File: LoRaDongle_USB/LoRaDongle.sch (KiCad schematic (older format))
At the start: 4 parts

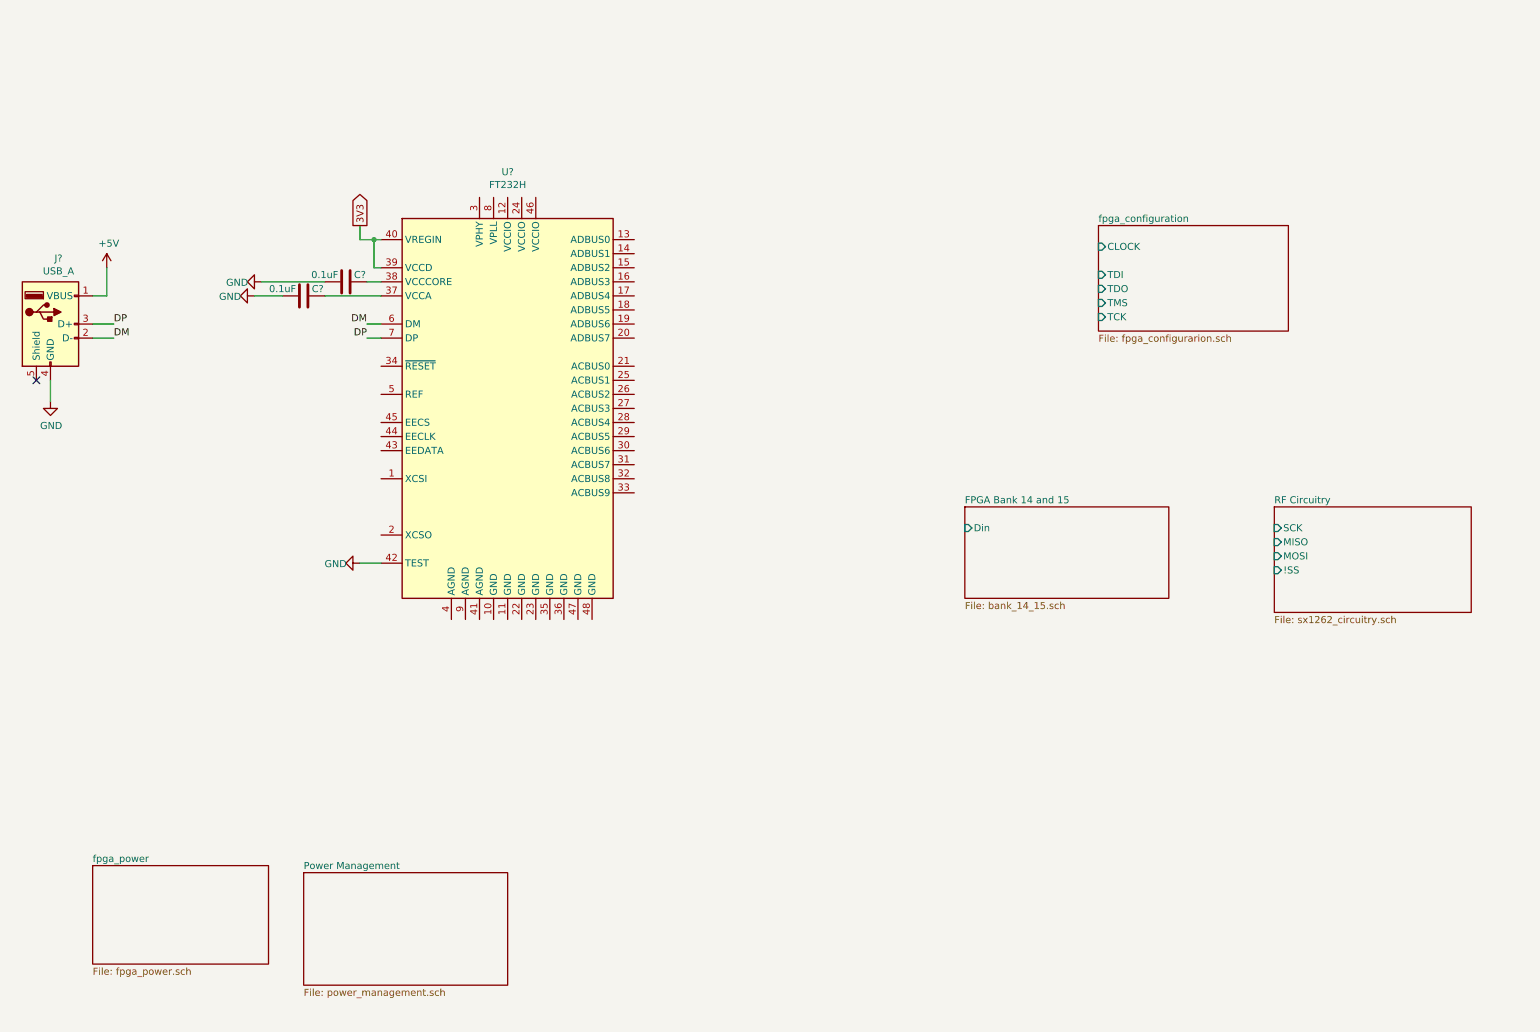
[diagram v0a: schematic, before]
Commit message: add eeprom
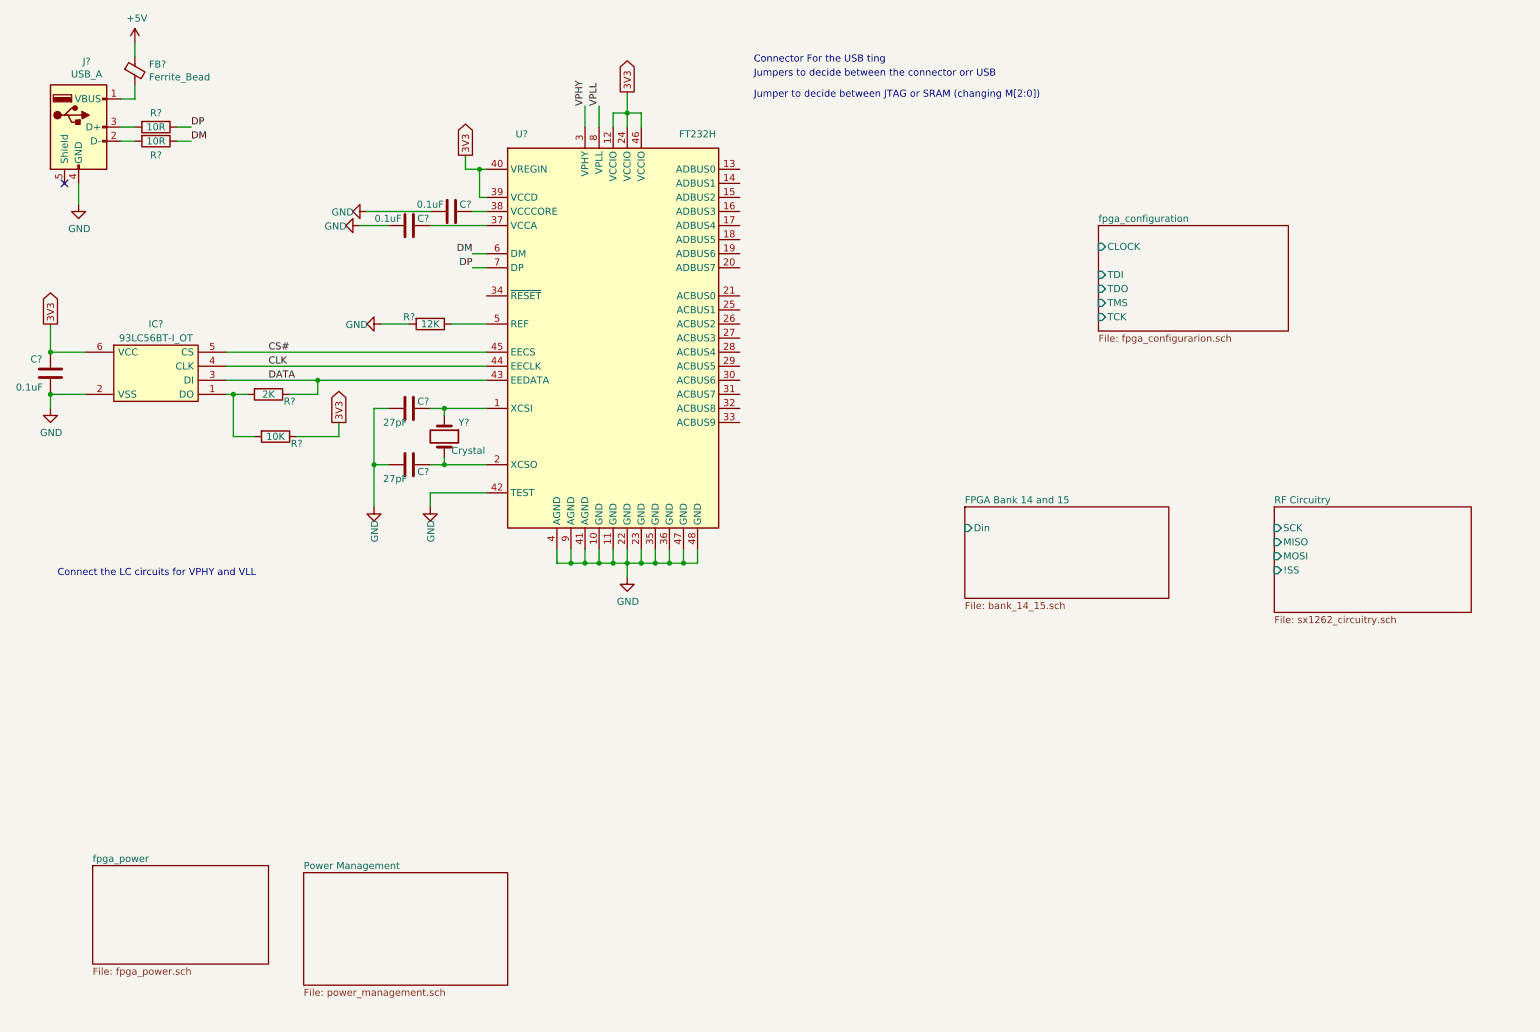
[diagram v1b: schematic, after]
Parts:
- added C?: 0.1uF, symbol Device:C
- added C? (x2): 27pF, Capacitor_SMD:C_0603_1608Metric, symbol Device:C
- added FB?: Ferrite_Bead, symbol Device:Ferrite_Bead_Small
- added IC?: 93LC56BT-I_OT, SOT95P270X145-6N, symbol 93LC56BT-I_OT:93LC56BT-I_OT
- added R?: 12K, symbol Device:R
- added R?: 2K, symbol Device:R
- added R?: 10K, symbol Device:R
- added R? (x2): 10R, symbol Device:R
- added Y?: Crystal, Crystal:Crystal_SMD_3225-4Pin_3.2x2.5mm, symbol Device:Crystal
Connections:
- net +5V: now also FB?.1; no longer J?.1 (VBUS)
- net 3V3: now also U?.12 (VCCIO), U?.24 (VCCIO), U?.46 (VCCIO), C?.2, IC?.6 (VCC), R?.1
- net DM: now also R?.1; no longer J?.2 (D-)
- net DP: now also R?.1; no longer J?.3 (D+)
- net GND: now also U?.10 (GND), U?.11 (GND), U?.22 (GND), U?.23 (GND), U?.35 (GND), U?.36 (GND), U?.4 (AGND), U?.41 (AGND), U?.47 (GND), U?.48 (GND), U?.9 (AGND), C?.1, C?.2, C?.2, IC?.2 (VSS), R?.2
- net at U?.1 (XCSI): now also C?.1, Y?.1
- net at U?.2 (XCSO): now also C?.1, Y?.2
- net VPHY: now reaches U?.3 (VPHY)
- net DATA: now reaches U?.43 (EEDATA)
- net DATA: now also IC?.3 (DI), R?.1
- net CLK: now reaches U?.44 (EECLK)
- net CLK: now also IC?.4 (CLK)
- net CS#: now reaches U?.45 (EECS)
- net CS#: now also IC?.5 (CS)
- net at U?.5 (REF): now also R?.1
- net VPLL: now reaches U?.8 (VPLL)
- new net: FB?.2, J?.1 (VBUS)
- new net: J?.2 (D-), R?.2
- new net: J?.3 (D+), R?.2
- new net: IC?.1 (DO), R?.2, R?.2
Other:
- note added: "Connect the LC circuits for VPHY and VLL"
- note added: "Connector For the USB ting"
- note added: "Jumper to decide between JTAG or SRAM (changing M[2:0])"
- note added: "Jumpers to decide between the connector orr USB"
- moved on the sheet: C?, J?, U?

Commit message: ft232h completed
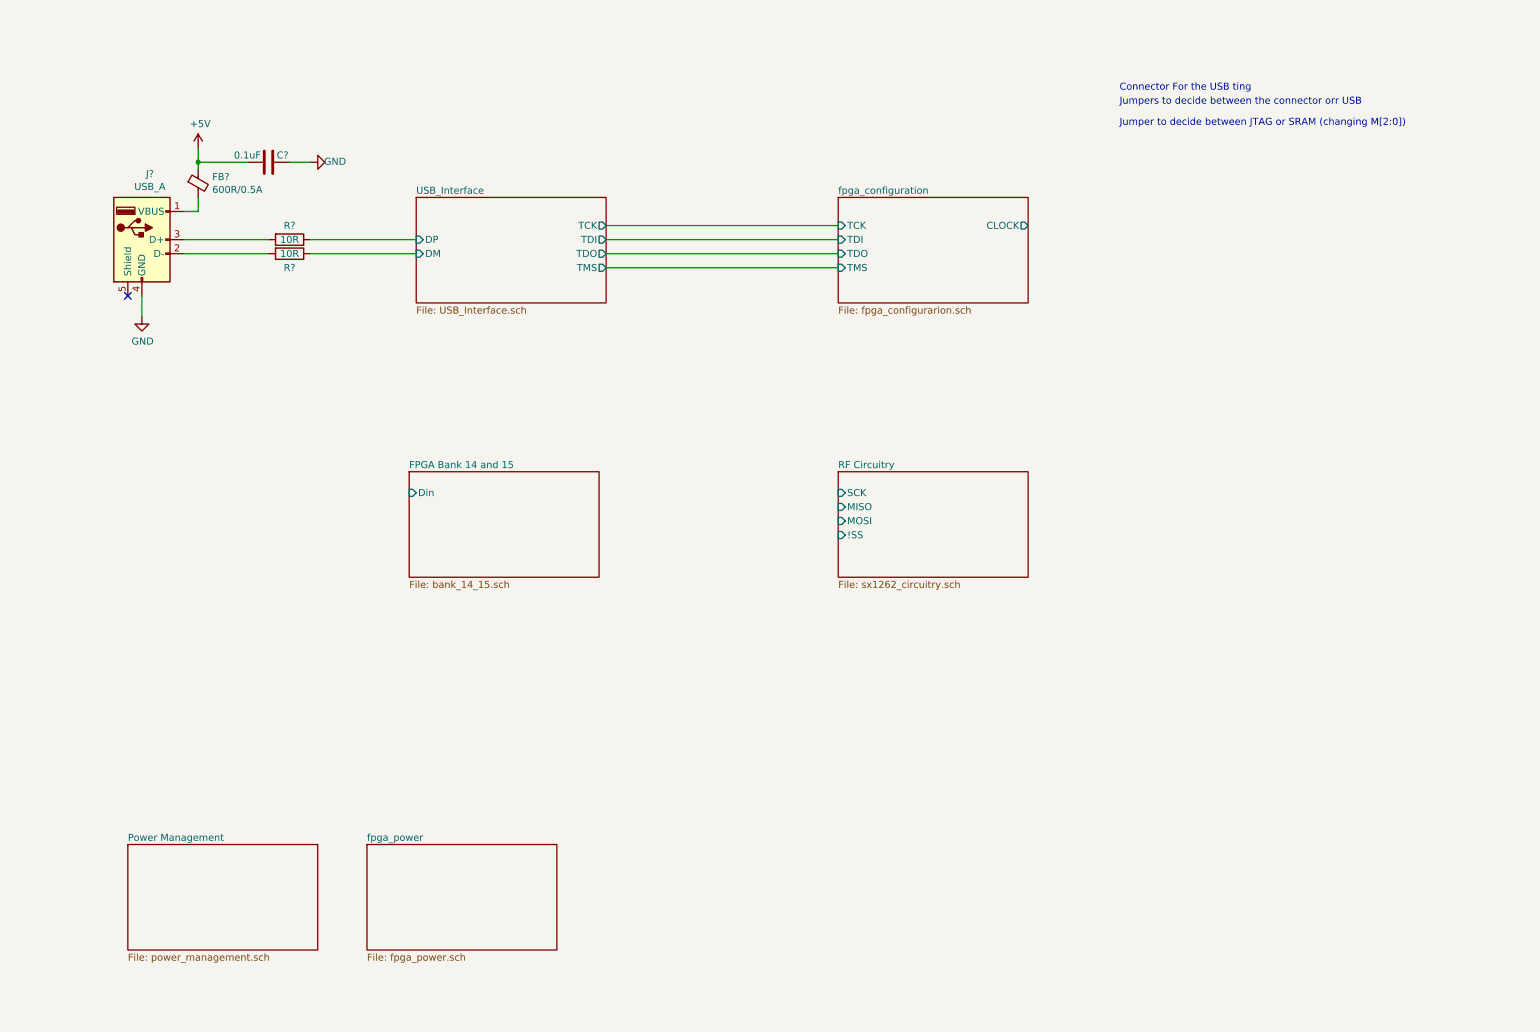
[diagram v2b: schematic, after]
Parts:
- removed C? (x3): 0.1uF, symbol Device:C
- removed C? (x2): 27pF, Capacitor_SMD:C_0603_1608Metric, symbol Device:C
- removed IC?: 93LC56BT-I_OT, SOT95P270X145-6N, symbol 93LC56BT-I_OT:93LC56BT-I_OT
- removed R?: 12K, symbol Device:R
- removed R?: 2K, symbol Device:R
- removed R?: 10K, symbol Device:R
- removed U?: FT232H, symbol Interface_USB:FT232H
- removed Y?: Crystal, Crystal:Crystal_SMD_3225-4Pin_3.2x2.5mm, symbol Device:Crystal
- added C?: 0.1uF, Capacitor_SMD:C_0402_1005Metric, symbol Device:C
- FB?: value Ferrite_Bead -> 600R/0.5A; footprint (none) -> digikey-footprints:0603; Part Number (none) -> 742863160
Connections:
- net +5V: now also C?.2
- net GND: now also C?.1
- net DM renamed USB_Interface/DM
- net DP renamed USB_Interface/DP
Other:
- note removed: "Connect the LC circuits for VPHY and VLL"
- moved on the sheet: FB?, J?, R?

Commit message: added flash memory configuration
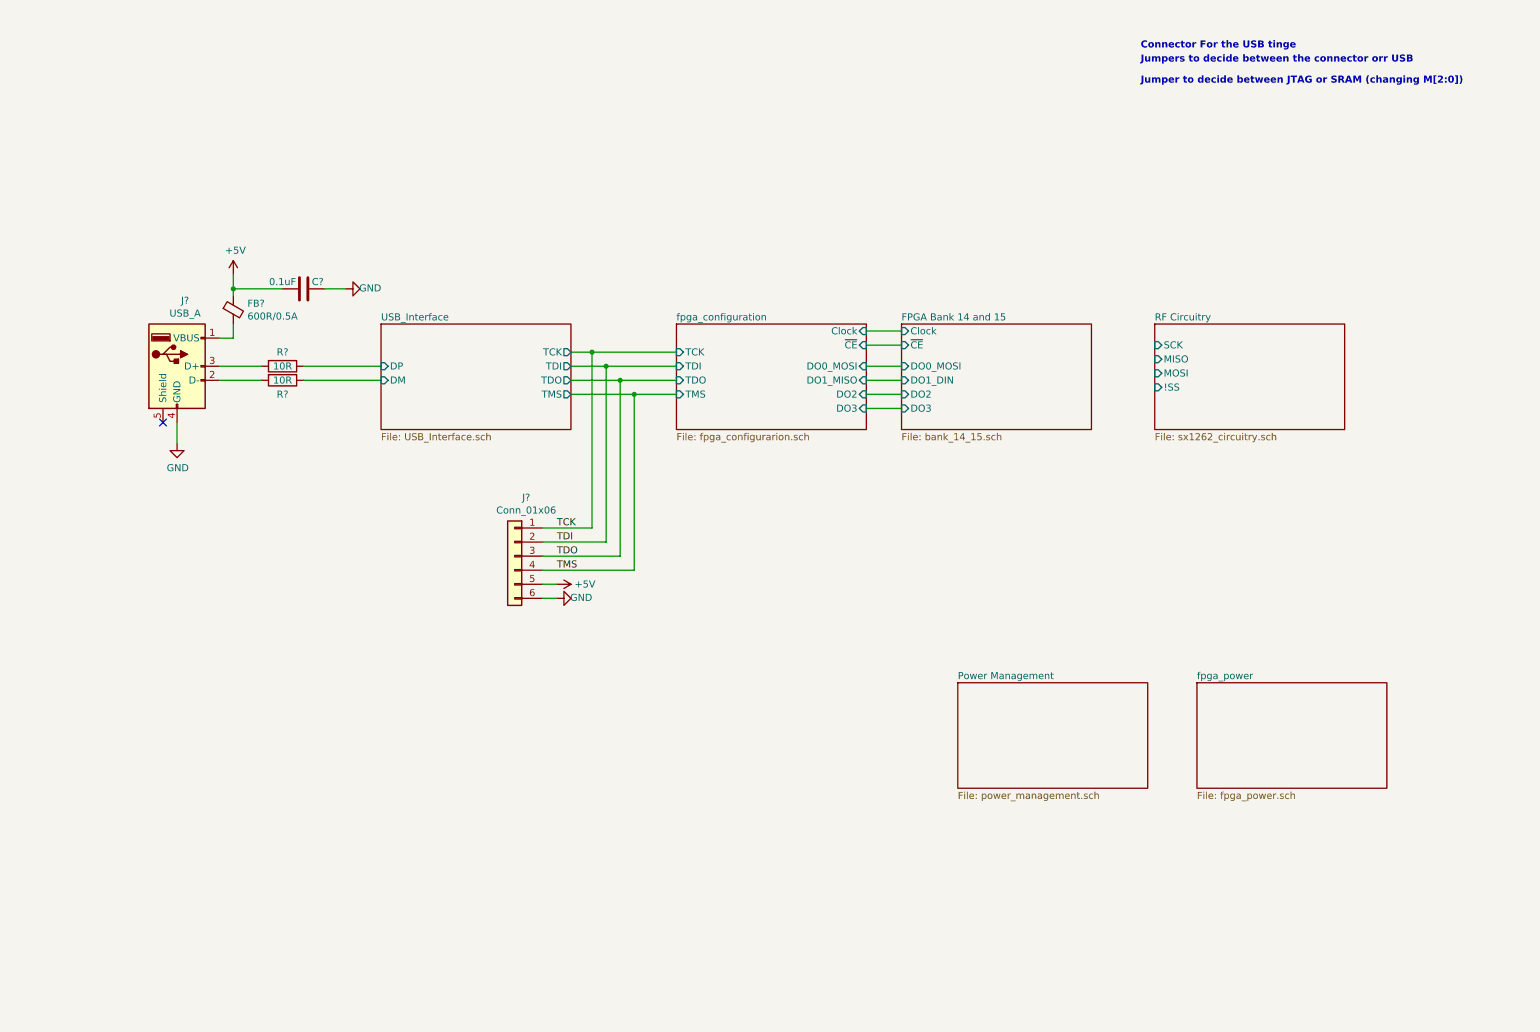
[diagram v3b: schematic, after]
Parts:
- added J?: Conn_01x06, symbol Connector_Generic:Conn_01x06
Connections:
- net +5V: now also J?.5 (Pin_5)
- net GND: now also J?.6 (Pin_6)
- new net TCK: J?.1 (Pin_1)
- new net TDI: J?.2 (Pin_2)
- new net TDO: J?.3 (Pin_3)
- new net TMS: J?.4 (Pin_4)
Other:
- note added: "Connector For the USB tinge"
- note removed: "Connector For the USB ting"
- moved on the sheet: C?, FB?, J?, R?

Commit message: updated RF circuitry
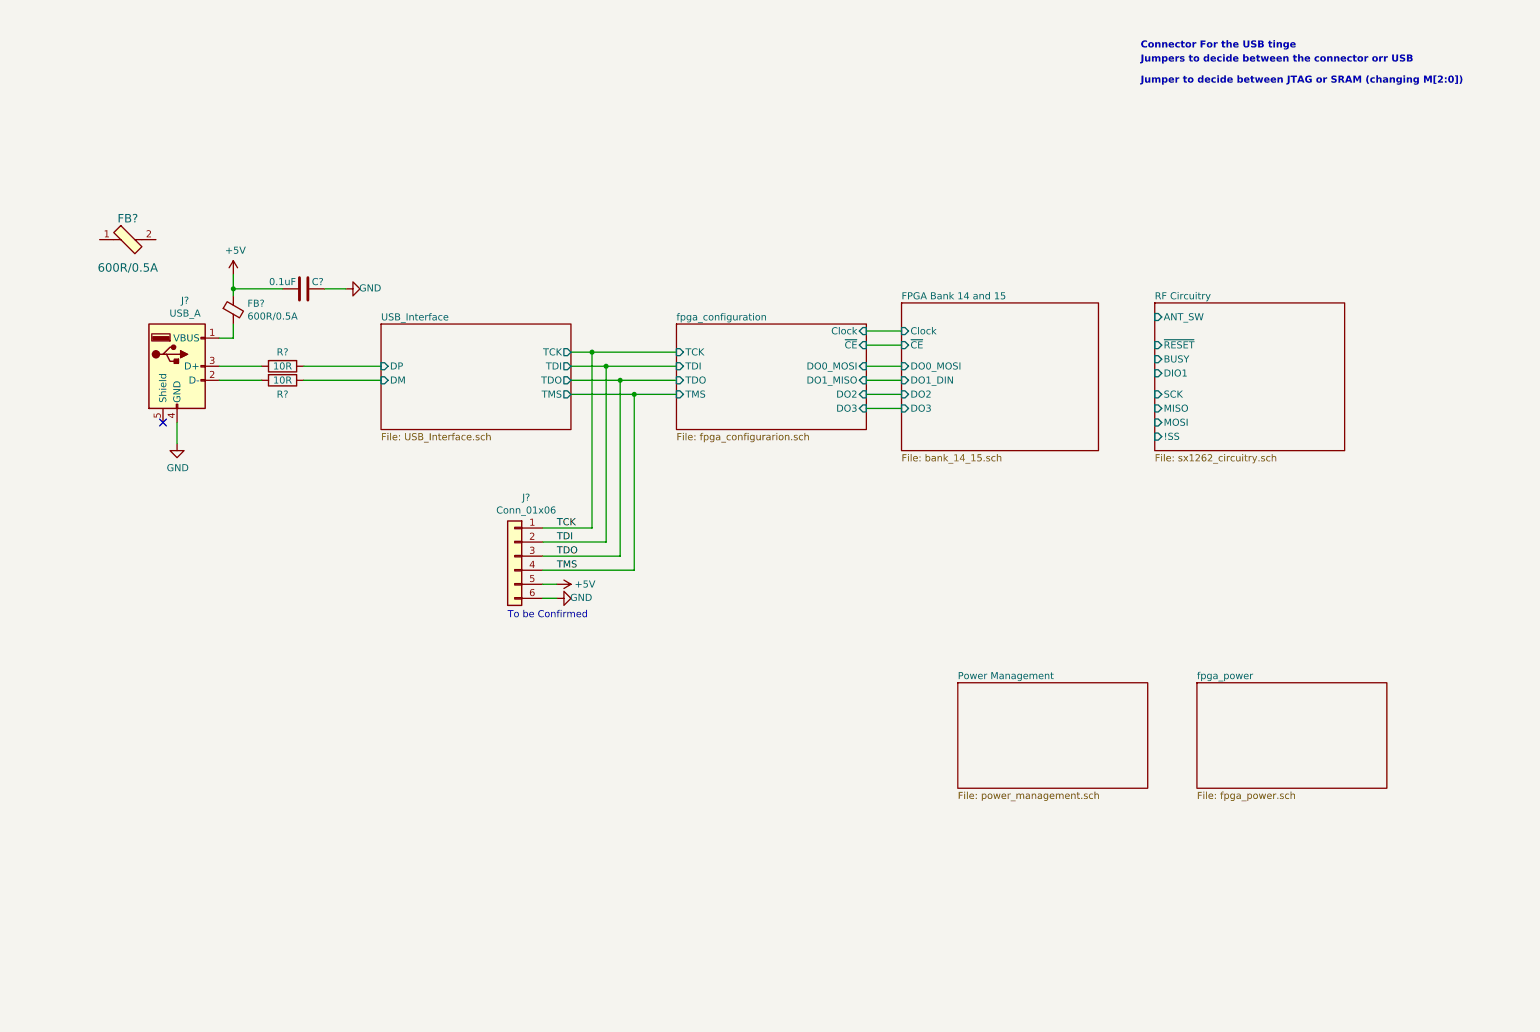
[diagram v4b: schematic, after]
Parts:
- added FB?: 600R/0.5A, digikey-footprints:0603, symbol dk_Ferrite-Beads-and-Chips:BLM18AG601SN1D
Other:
- note added: "To be Confirmed"
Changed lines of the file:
@@
 $EndDescr
-$Sheet
-S 8700 2750 1350 750
-U 614F0720
-F0 "RF Circuitry" 50
-F1 "sx1262_circuitry.sch" 50
-F2 "SCK" I L 8700 2900 50
-F3 "MISO" I L 8700 3000 50
-F4 "MOSI" I L 8700 3100 50
-F5 "!SS" I L 8700 3200 50
-$EndSheet
 $Sheet
 S 7300 5300 1350 750
@@
 F0 "fpga_power" 50
 F1 "fpga_power.sch" 50
-$EndSheet
-$Sheet
-S 6900 2750 1350 750
-U 61611C59
-F0 "FPGA Bank 14 and 15" 50
-F1 "bank_14_15.sch" 50
-F2 "DO0_MOSI" I L 6900 3050 50
-F3 "Clock" I L 6900 2800 50
-F4 "~CE" I L 6900 2900 50
-F5 "DO1_DIN" I L 6900 3150 50
-F6 "DO2" I L 6900 3250 50
-F7 "DO3" I L 6900 3350 50
 $EndSheet
 Text Notes 8600 800  0    50   ~ 10
@@
 Wire Wire Line
 	6650 2800 6900 2800
+Text Notes 4100 4850 0    50   ~ 0
+To be Confirmed
+$Comp
+L dk_Ferrite-Beads-and-Chips:BLM18AG601SN1D FB?
+U 1 1 615E0B04
+P 1400 2150
+F 0 "FB?" H 1400 2300 60  0000 C CNN
+F 1 "600R/0.5A" H 1400 1950 60  0000 C CNN
+F 2 "digikey-footprints:0603" H 1600 2350 60  0001 L CNN
+F 3 "https://www.murata.com/en-us/products/productdata/8796738650142/ENFA0003.pdf" H 1600 2450 60  0001 L CNN
+F 4 "490-1014-1-ND" H 1600 2550 60  0001 L CNN "Digi-Key_PN"
+F 5 "BLM18AG601SN1D" H 1600 2650 60  0001 L CNN "MPN"
+F 6 "Filters" H 1600 2750 60  0001 L CNN "Category"
+F 7 "Ferrite Beads and Chips" H 1600 2850 60  0001 L CNN "Family"
+F 8 "https://www.murata.com/en-us/products/productdata/8796738650142/ENFA0003.pdf" H 1600 2950 60  0001 L CNN "DK_Datasheet_Link"
+F 9 "/product-detail/en/murata-electronics-north-america/BLM18AG601SN1D/490-1014-1-ND/584462" H 1600 3050 60  0001 L CNN "DK_Detail_Page"
+F 10 "FERRITE BEAD 600 OHM 0603 1LN" H 1600 3150 60  0001 L CNN "Description"
+F 11 "Murata Electronics North America" H 1600 3250 60  0001 L CNN "Manufacturer"
+F 12 "Active" H 1600 3350 60  0001 L CNN "Status"
+	1    1400 2150
+	1    0    0    -1
+$EndComp
+$Sheet
+S 8700 2600 1350 1050
+U 614F0720
+F0 "RF Circuitry" 50
+F1 "sx1262_circuitry.sch" 50
+F2 "SCK" I L 8700 3250 50
+F3 "MISO" I L 8700 3350 50
+F4 "MOSI" I L 8700 3450 50
+F5 "!SS" I L 8700 3550 50
+F6 "ANT_SW" I L 8700 2700 50
+F7 "~RESET" I L 8700 2900 50
+F8 "BUSY" I L 8700 3000 50
+F9 "DIO1" I L 8700 3100 50
+$EndSheet
+$Sheet
+S 6900 2600 1400 1050
+U 61611C59
+F0 "FPGA Bank 14 and 15" 50
+F1 "bank_14_15.sch" 50
+F2 "DO0_MOSI" I L 6900 3050 50
+F3 "Clock" I L 6900 2800 50
+F4 "~CE" I L 6900 2900 50
+F5 "DO1_DIN" I L 6900 3150 50
+F6 "DO2" I L 6900 3250 50
+F7 "DO3" I L 6900 3350 50
+$EndSheet
 $EndSCHEMATC
